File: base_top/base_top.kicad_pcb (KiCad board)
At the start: 2 copper layers, 92 x 40 mm, 0 parts

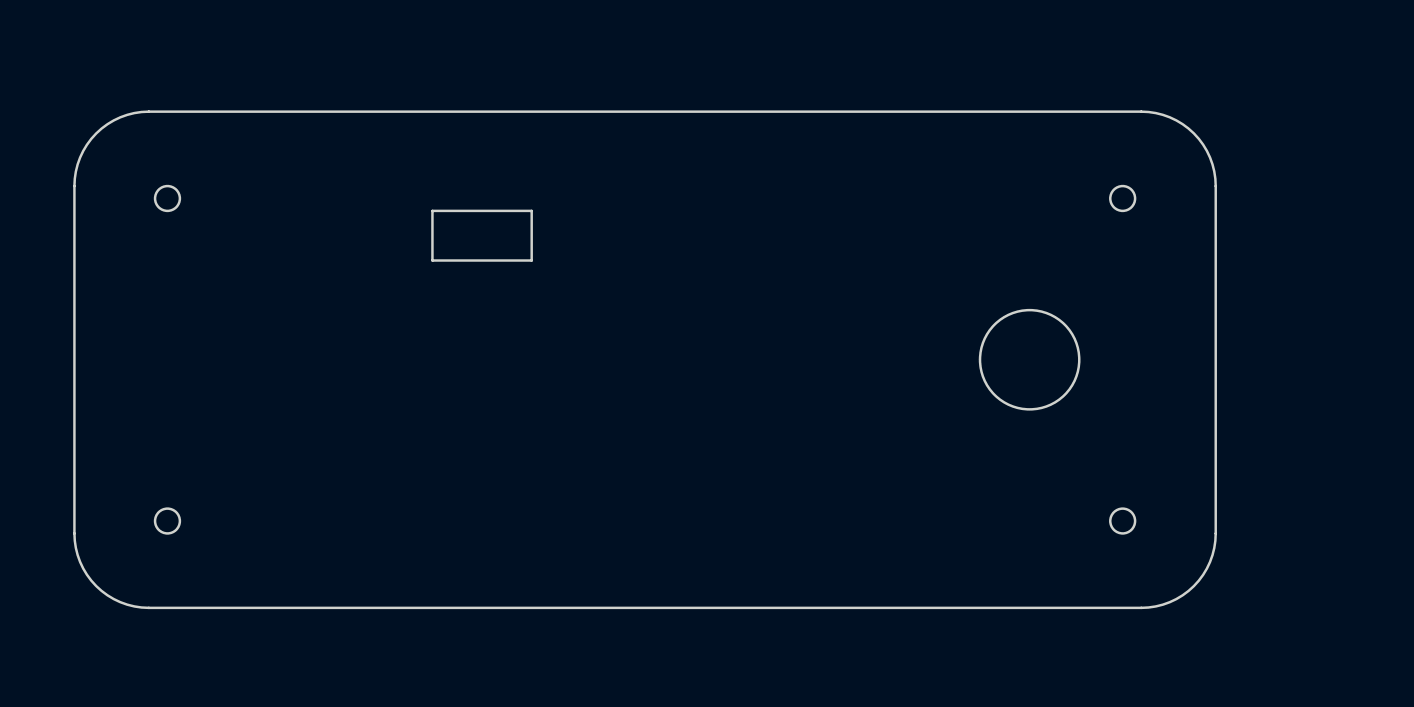
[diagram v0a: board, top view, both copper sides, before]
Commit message: Add copper zone to base_top
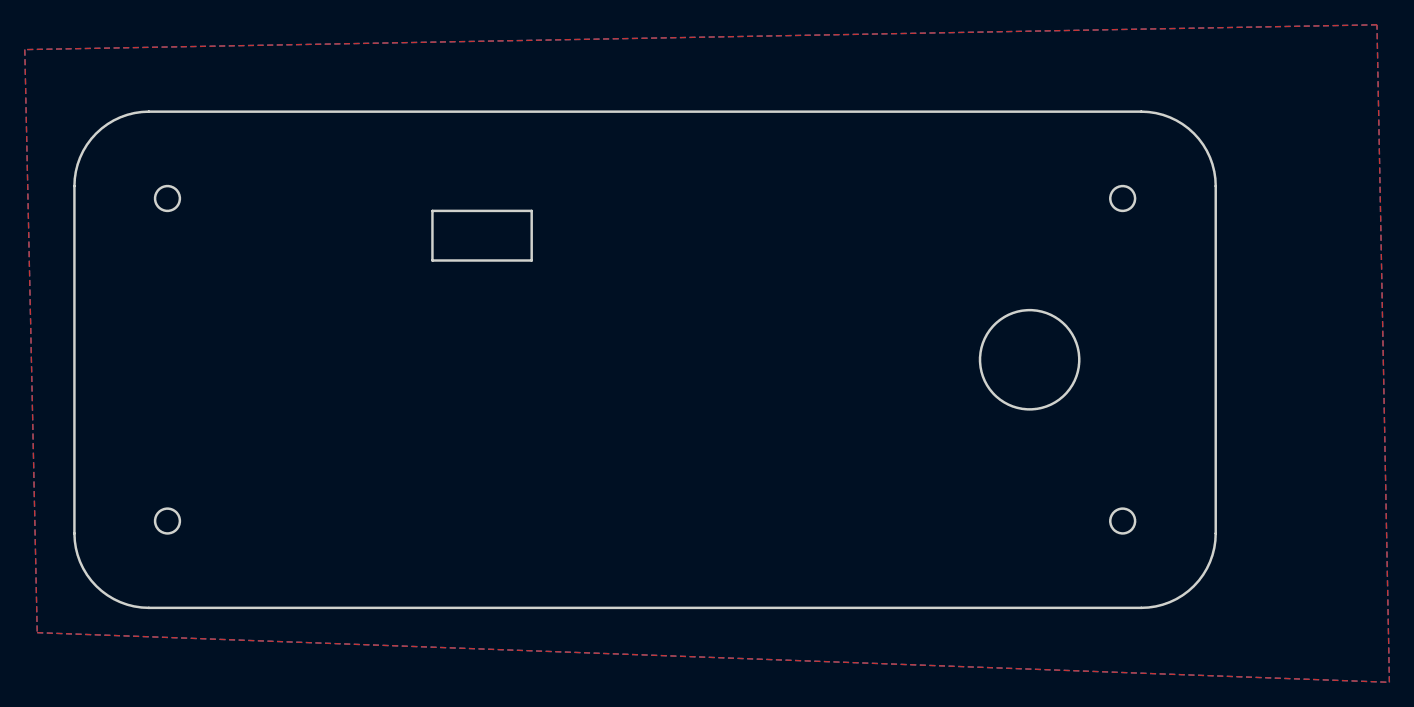
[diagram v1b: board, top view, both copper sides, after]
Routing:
- added copper zone on B.Cu, net (none)
- added copper zone on F.Cu, net (none)
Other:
- board text added: "FOCUS"
- board text added: "maybe..."

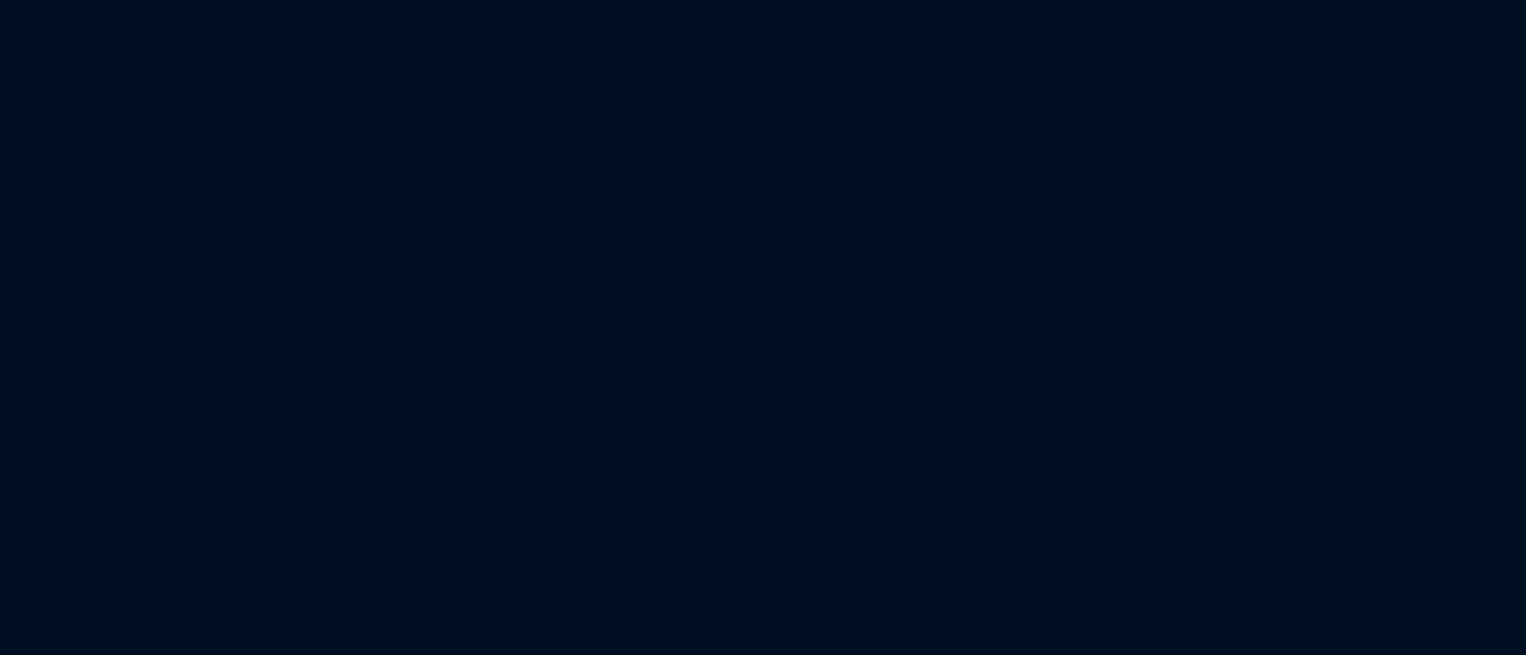
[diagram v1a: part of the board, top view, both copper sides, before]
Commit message: feat: Update PCB design settings and rules in KiCad project file
- Enhanced design settings with default values for various parameters including line widths, text sizes, and dimensions.
- Added detailed rule severities for various design checks to improve error handling.
- Introduced teardrop options and parameters for better track and pad connections.
- Updated tuning pattern settings for differential pairs and single tracks.

chore: Update project dependencies in pyproject.toml

- Added dotenv and pydantic as dependencies with specified versions.

feat: Create common utility functions for path validation

- Introduced a new script (common.py) with a function to validate file and directory paths.

feat: Implement mounting hole addition script

- Created mh_add.py to add mounting holes to PCB files based on specified coordinates and footprint.

feat: Implement mounting hole deletion script

- Created mh_delete_all.py to remove all generated mounting holes from a PCB file.

chore: Update lock file with new dependencies

- Updated uv.lock to include new packages and their versions.
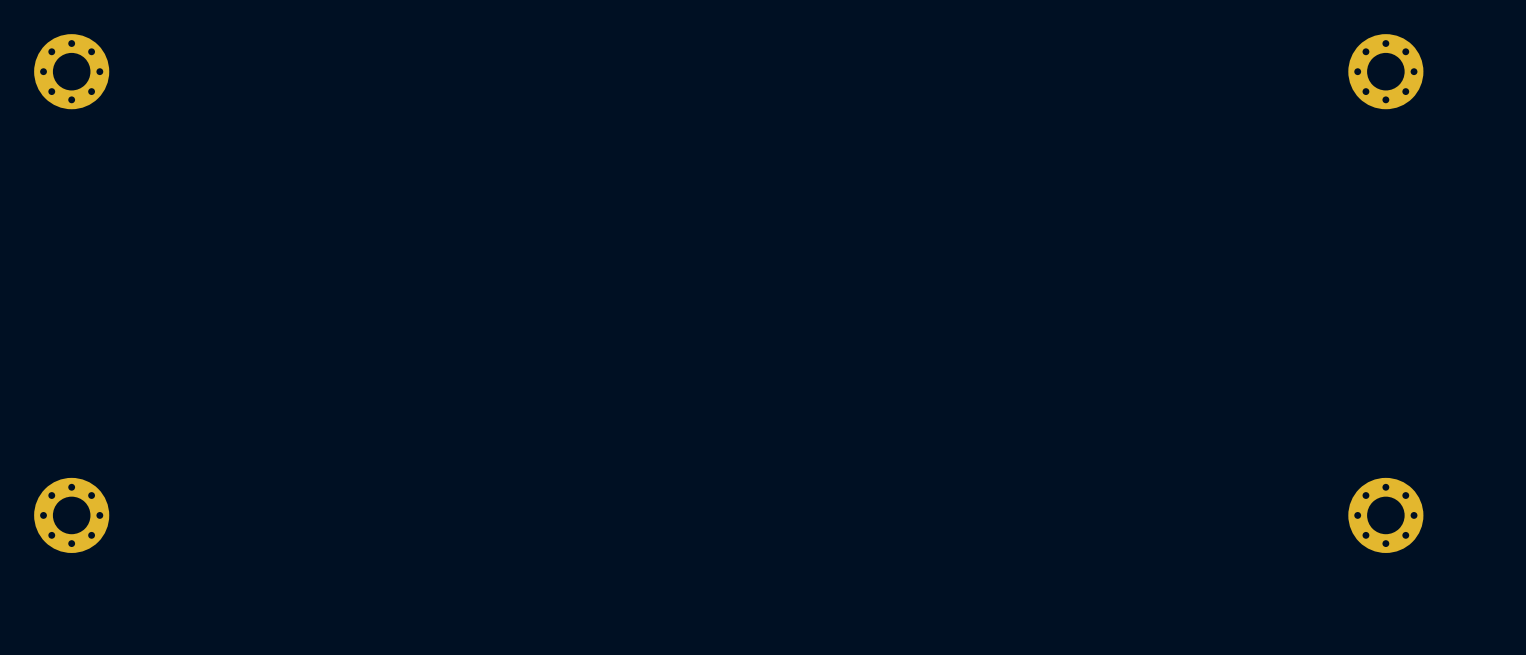
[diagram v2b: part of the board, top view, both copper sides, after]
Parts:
- added generated: MountingHole_2.2mm_M2_Pad_Via, MountingHole_2.2mm_M2_Pad_Via, F.Cu at (77.0, 0.00)
- added generated: MountingHole_2.2mm_M2_Pad_Via, MountingHole_2.2mm_M2_Pad_Via, F.Cu at (0.00, 0.00)
- added generated: MountingHole_2.2mm_M2_Pad_Via, MountingHole_2.2mm_M2_Pad_Via, F.Cu at (77.0, 26.0)
- added generated: MountingHole_2.2mm_M2_Pad_Via, MountingHole_2.2mm_M2_Pad_Via, F.Cu at (0.00, 26.0)
